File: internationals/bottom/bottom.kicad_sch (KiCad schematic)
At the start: 67 parts, among them J1 JST-XH-B6B, J2 Header-01x09, J3 3.3V-JST-XH-B2B, J4 JST-XH-B4B, J5 3.3V-JST-XH-B2B, J6 3.3V-JST-XH-B2B, J7 3.3V-JST-XH-B2B, U1 ESP-S2-Pico, U2 MINI560 3.3V

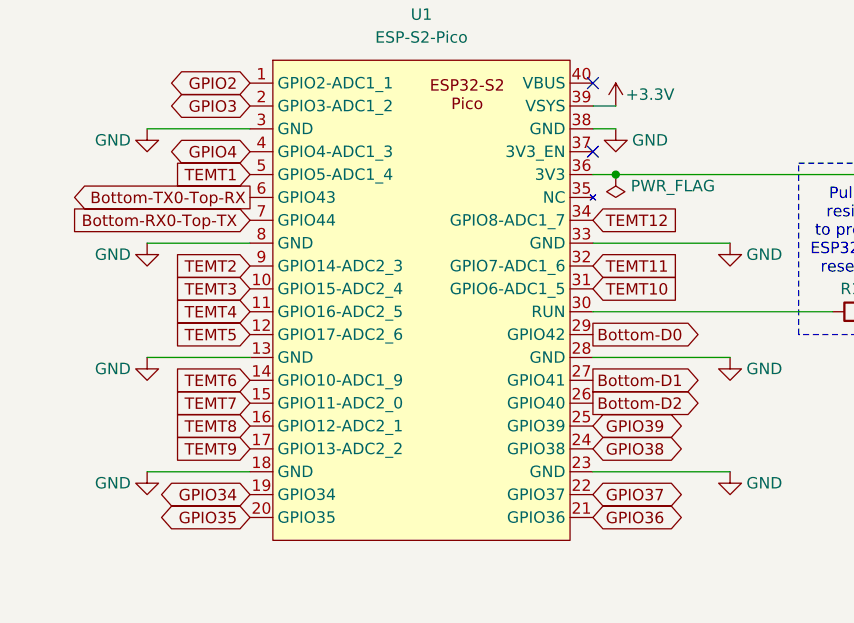
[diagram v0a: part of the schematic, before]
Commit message: pcbs: bottom: feat: complete pcb routing, update schematics with better TEMT allocation
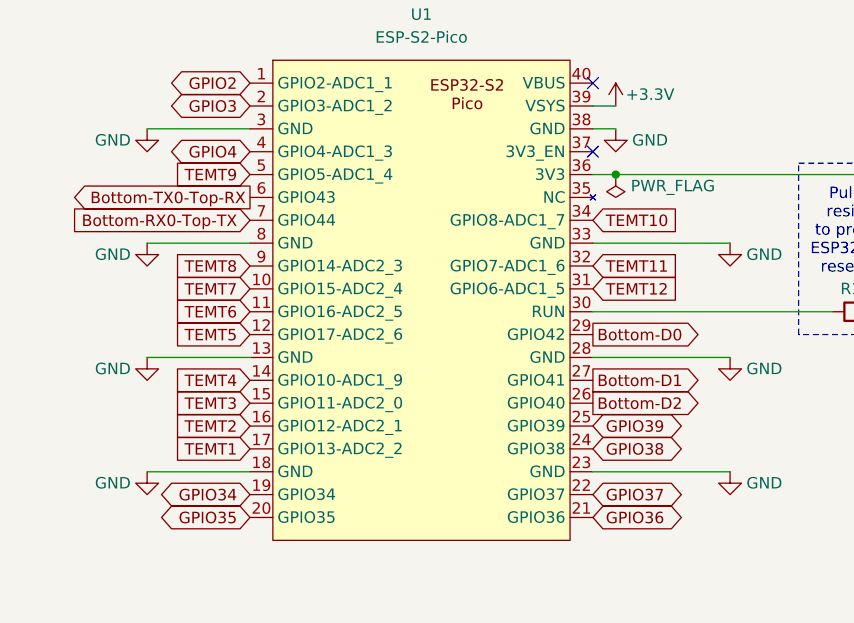
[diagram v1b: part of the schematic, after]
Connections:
- net TEMT1: now also U1.17 (GPIO13-ADC2_2); no longer U1.5 (GPIO5-ADC1_4)
- net TEMT10: now also U1.34 (GPIO8-ADC1_7); no longer U1.31 (GPIO6-ADC1_5)
- net TEMT12: now also U1.31 (GPIO6-ADC1_5); no longer U1.34 (GPIO8-ADC1_7)
- net TEMT2: now also U1.16 (GPIO12-ADC2_1); no longer U1.9 (GPIO14-ADC2_3)
- net TEMT3: now also U1.15 (GPIO11-ADC2_0); no longer U1.10 (GPIO15-ADC2_4)
- net TEMT4: now also U1.14 (GPIO10-ADC1_9); no longer U1.11 (GPIO16-ADC2_5)
- net TEMT6: now also U1.11 (GPIO16-ADC2_5); no longer U1.14 (GPIO10-ADC1_9)
- net TEMT7: now also U1.10 (GPIO15-ADC2_4); no longer U1.15 (GPIO11-ADC2_0)
- net TEMT8: now also U1.9 (GPIO14-ADC2_3); no longer U1.16 (GPIO12-ADC2_1)
- net TEMT9: now also U1.5 (GPIO5-ADC1_4); no longer U1.17 (GPIO13-ADC2_2)
